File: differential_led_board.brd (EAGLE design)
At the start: 72 x 117 mm, 59 parts, among them IC1 SN75175SOP-16, IC10 TJA1057, IC3 LD1117S33, IC4 74LVC1G157, IC5 74LVC1G157, IC6 CD40109B, IC7 STM32F042F, IC8 AT25SF041, IC9 LT6100, J1 CORTEX_DEBUG_PTH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

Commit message: yes
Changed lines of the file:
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@@
 <attribute name="SPICEPREFIX" value="C" x="13.208" y="103.0732" size="1.778" layer="27" rot="R270" display="off"/>
 </element>
-<element name="IC3" library="lichtenstein_onion" package="SOT223" value="LD1117S33" x="16.3322" y="89.2302" smashed="yes" rot="R180">
+<element name="IC3" library="lichtenstein_onion" package="SOT223" package3d_urn="urn:adsk.eagle:package:29214/2" value="LD1117S33" x="16.3322" y="89.2302" smashed="yes" rot="R180">
 <attribute name="MOUSER" value="926-LM1117MPX3.3NOPB" x="16.3322" y="89.2302" size="1.778" layer="27" rot="R180" display="off"/>
 <attribute name="NAME" x="12.5857" y="87.7443" size="0.8128" layer="25" font="vector" ratio="10" rot="R90"/>

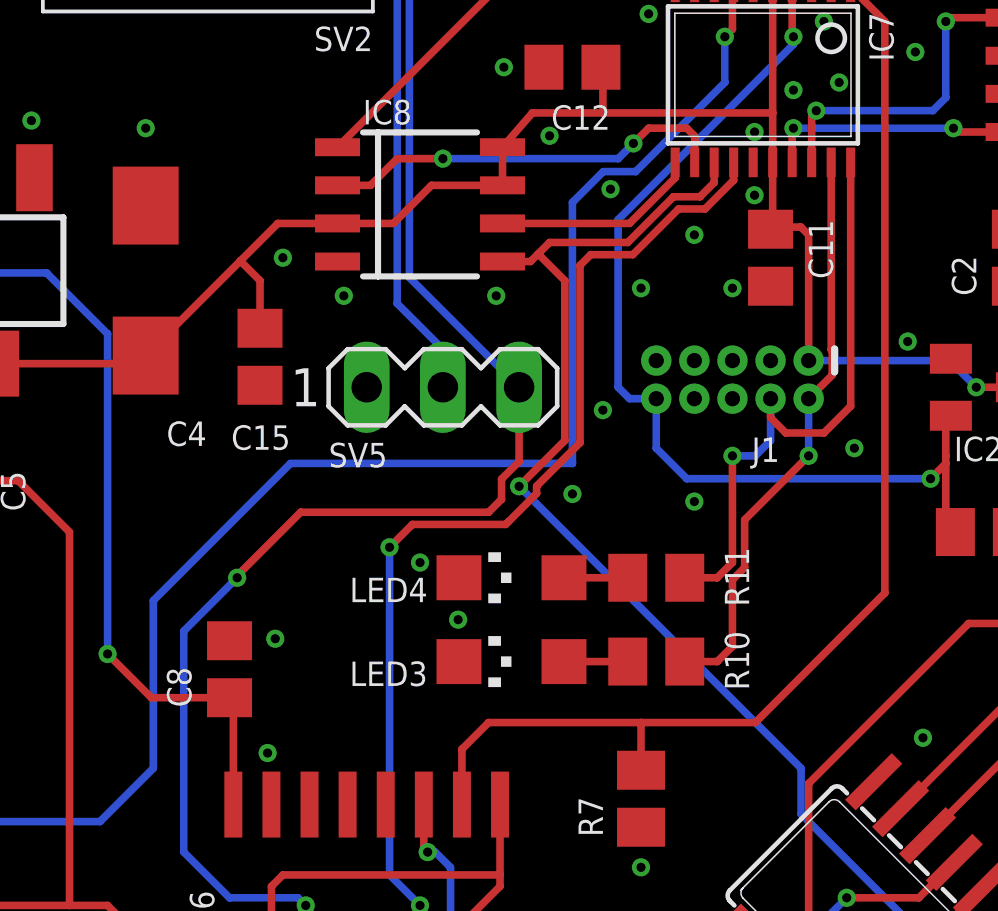
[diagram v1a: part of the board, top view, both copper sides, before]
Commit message: moved status LEDs from debug pins to SPI pins
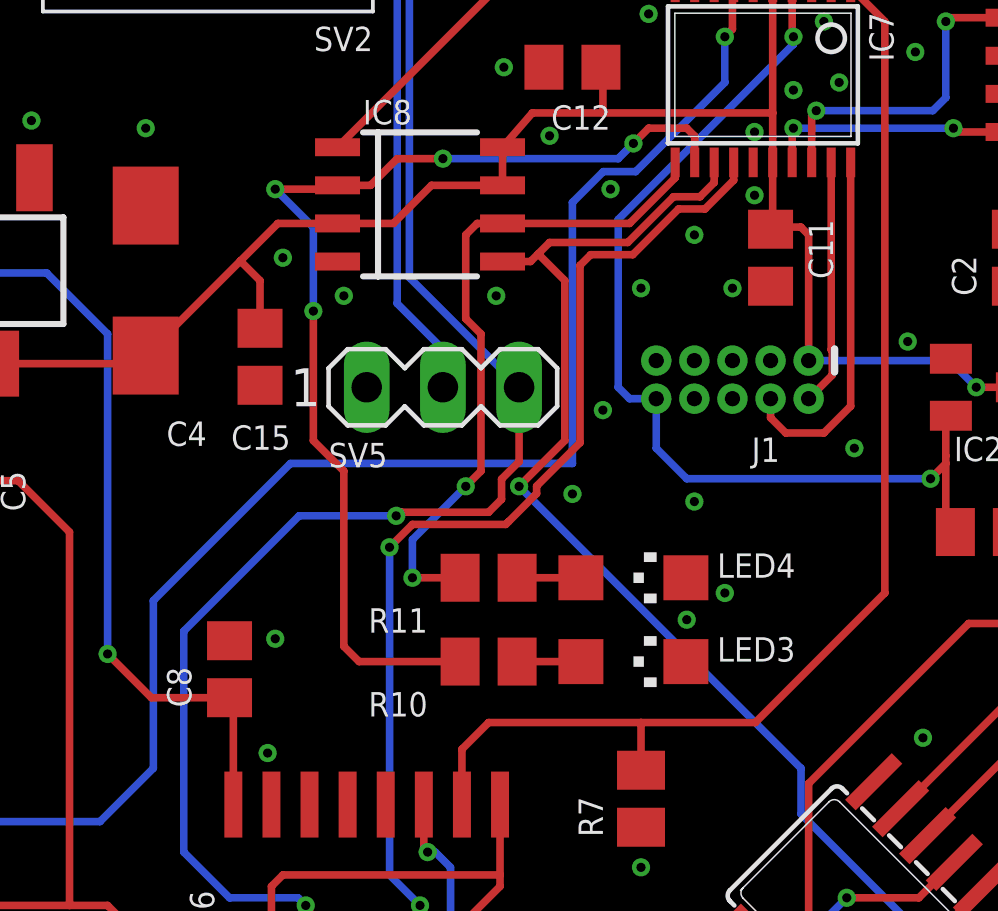
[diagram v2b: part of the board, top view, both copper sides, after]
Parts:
- moved R10 5.59 mm to (33.8, 76.2), turned to 0 degrees
- moved R11 5.59 mm to (33.8, 79.0), turned to 0 degrees
- moved LED3 4.06 mm to (38.6, 76.2), turned to 270 degrees
- moved LED4 4.06 mm to (38.6, 79.0), turned to 270 degrees
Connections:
- net CORTEX_SWCLK: no longer R11.1
- net CORTEX_SWDIO: no longer R10.1
- net SPI_MISO: now also R10.1
- net SPI_SCK: now also R11.1
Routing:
- net SPI_MISO: track 13.7 -> 36.3 mm, vias 2 -> 4
- net SPI_SCK: track 6.90 -> 22.5 mm, vias 0 -> 2
- net CORTEX_SWDIO: track 19.3 -> 8.22 mm, vias 1 -> 0
- net CORTEX_SWCLK: track 20.2 -> 12.0 mm, vias 1 -> 0

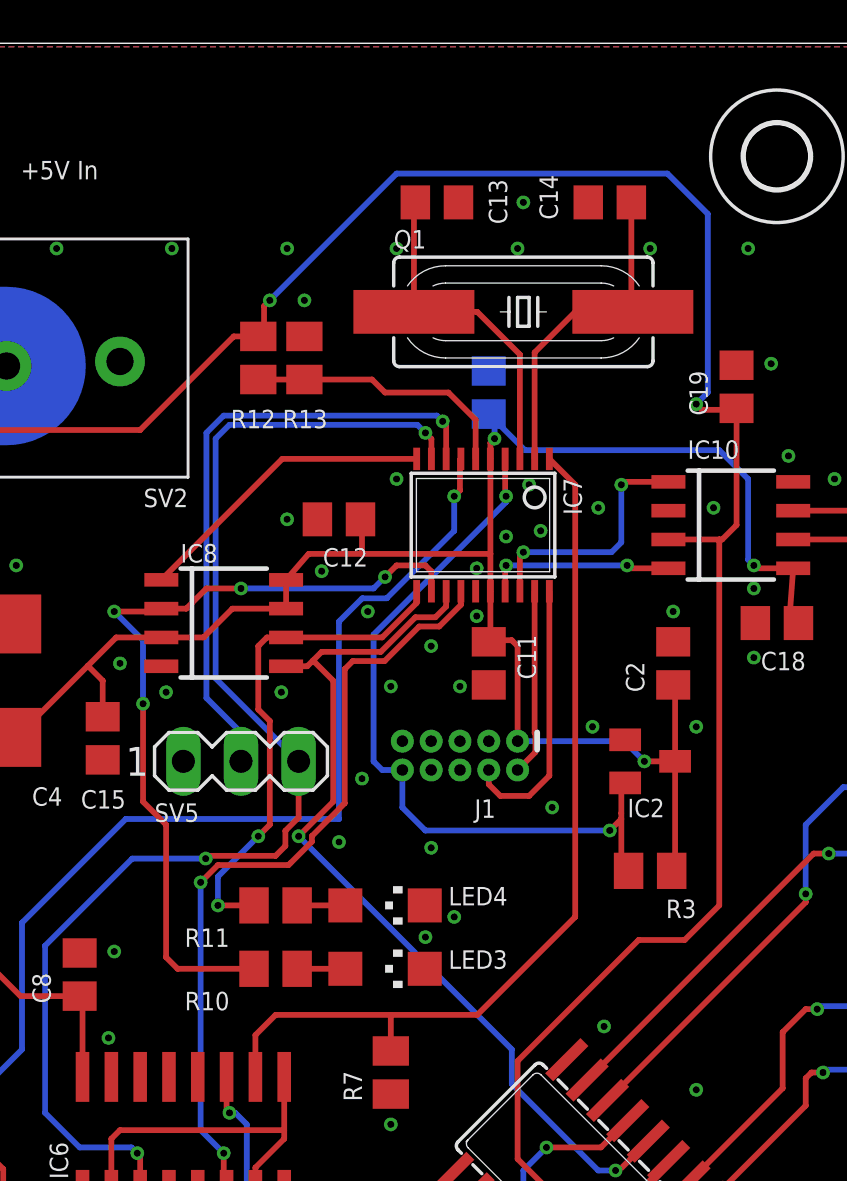
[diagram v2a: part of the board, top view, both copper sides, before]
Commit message: submitted rev 1 of output and led boards to board house
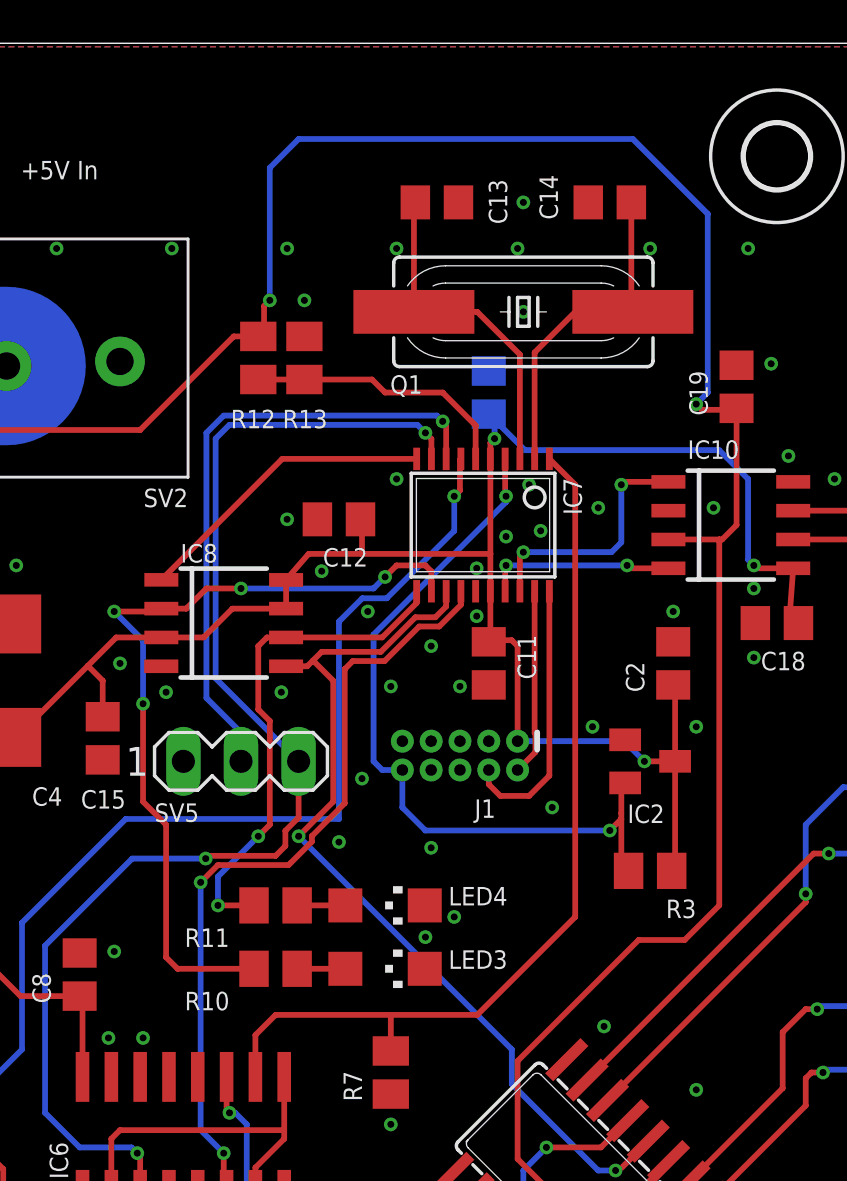
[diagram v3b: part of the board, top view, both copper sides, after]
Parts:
- IC1: value SN75175SOP-16 -> SN75175
- IC2: value (none) -> TLV803
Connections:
- net GND: now also IC6.14
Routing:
- net +5V: track 345.2 -> 349.9 mm
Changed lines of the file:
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@@
 </class>
 </classes>
-<designrules name="dirt_cheap_dirty_boards.v1.1 *">
+<designrules name="dirt_cheap_dirty_boards.v1.1">
 <description language="de">&lt;b&gt;Dirty Cheap Dirty Board Design Rules&lt;/b&gt;
 &lt;br&gt;
@@
 <param name="checkValues" value="0"/>
 <param name="checkNames" value="1"/>
-<param name="checkWireStubs" value="0"/>
+<param name="checkWireStubs" value="1"/>
 <param name="checkPolygonWidth" value="0"/>
 <param name="useDiameter" value="13"/>
@@
 <attribute name="MOUSER" value="449-LFXTAL030234REEL" x="44.704" y="105.156" size="1.778" layer="27" display="off"/>
 <attribute name="MPN" value="" x="44.704" y="105.156" size="1.778" layer="27" display="off"/>
-<attribute name="NAME" x="38.989" y="107.95" size="0.8128" layer="25" font="vector" ratio="10"/>
+<attribute name="NAME" x="40.259" y="102.362" size="0.8128" layer="25" font="vector" ratio="10" rot="R180"/>
 <attribute name="OC_FARNELL" value="unknown" x="44.704" y="105.156" size="1.778" layer="27" display="off"/>
 <attribute name="OC_NEWARK" value="unknown" x="44.704" y="105.156" size="1.778" layer="27" display="off"/>
@@
 <attribute name="SPICEPREFIX" value="C" x="48.514" y="109.982" size="1.778" layer="27" display="off"/>
 </element>
-<element name="IC1" library="lichtenstein_onion" package="SOP-16" value="SN75175SOP-16" x="47.244" y="66.548" smashed="yes" rot="R135">
+<element name="IC1" library="lichtenstein_onion" package="SOP-16" value="SN75175" x="47.244" y="66.548" smashed="yes" rot="R135">
 <attribute name="MOUSER" value="595-SN75175DR" x="47.244" y="66.548" size="1.778" layer="27" rot="R135" display="off"/>
 <attribute name="NAME" x="53.081165625" y="64.302934375" size="0.8128" layer="25" font="vector" ratio="10" rot="R225"/>
@@
 <attribute name="NAME" x="24.638" y="66.929" size="0.8128" layer="25" font="vector" ratio="10" rot="R90"/>
 </element>
-<element name="IC2" library="lichtenstein_onion" package="SOT23" package3d_urn="urn:adsk.eagle:package:28738/2" value="" x="50.292" y="85.344" smashed="yes" rot="R270">
+<element name="IC2" library="lichtenstein_onion" package="SOT23" package3d_urn="urn:adsk.eagle:package:28738/2" value="TLV803" x="50.292" y="85.344" smashed="yes" rot="R270">
 <attribute name="MOUSER" value="595-TLV803SDBZR" x="50.292" y="85.344" size="0.8128" layer="27" font="vector" ratio="10" rot="R270" display="off"/>
-<attribute name="NAME" x="50.927" y="83.693" size="0.8128" layer="25" ratio="10" rot="R180"/>
+<attribute name="NAME" x="50.927" y="83.439" size="0.8128" layer="25" ratio="10" rot="R180"/>
 <attribute name="VALUE" x="47.117" y="87.249" size="1.27" layer="27" rot="R270"/>
 </element>
@@
 <via x="48.006" y="96.52" extent="1-16" drill="0.3048"/>
 <via x="44.704" y="109.982" extent="1-16" drill="0.3048"/>
+<via x="44.704" y="105.156" extent="1-16" drill="0.3048"/>
+<contactref element="IC6" pad="14"/>
+<via x="27.94" y="73.152" extent="1-16" drill="0.3048"/>
 </signal>
 <signal name="+5V">
@@
 <wire x1="33.274" y1="105.41" x2="33.528" y2="105.664" width="0.254" layer="1"/>
 <via x="33.528" y="105.664" extent="1-16" drill="0.3048"/>
-<wire x1="33.528" y1="105.664" x2="39.116" y2="111.252" width="0.254" layer="16"/>
 <wire x1="52.832" y1="101.6" x2="52.324" y2="101.092" width="0.254" layer="16"/>
 <via x="52.324" y="101.092" extent="1-16" drill="0.3048"/>
@@
 <wire x1="52.578" y1="100.838" x2="54.036" y2="100.838" width="0.254" layer="1"/>
 <wire x1="54.036" y1="100.838" x2="54.102" y2="100.904" width="0.254" layer="1"/>
-<wire x1="39.116" y1="111.252" x2="51.054" y2="111.252" width="0.254" layer="16"/>
-<wire x1="51.054" y1="111.252" x2="52.832" y2="109.474" width="0.254" layer="16"/>
+<wire x1="52.832" y1="109.474" x2="49.53" y2="112.776" width="0.254" layer="16"/>
 <wire x1="52.832" y1="109.474" x2="52.832" y2="101.6" width="0.254" layer="16"/>
 <wire x1="47.876859375" y1="60.89468125" x2="50.128246875" y2="58.64329375" width="0.254" layer="1"/>
@@
 <wire x1="51.816" y1="77.47" x2="53.34" y2="78.994" width="0.254" layer="1"/>
 <wire x1="53.34" y1="78.994" x2="53.34" y2="95.123" width="0.254" layer="1"/>
+<wire x1="34.798" y1="112.776" x2="33.528" y2="111.506" width="0.254" layer="16"/>
+<wire x1="49.53" y1="112.776" x2="34.798" y2="112.776" width="0.254" layer="16"/>
+<wire x1="33.528" y1="111.506" x2="33.528" y2="105.664" width="0.254" layer="16"/>
 </signal>
 <signal name="N$1">
@@
 <wire x1="33.02" y1="102.174" x2="35.052" y2="102.174" width="0.254" layer="1"/>
 <wire x1="35.052" y1="102.174" x2="38.034" y2="102.174" width="0.254" layer="1"/>
-<wire x1="42.601" y1="100.401" x2="42.601" y2="98.6758" width="0.254" layer="1"/>
+<wire x1="42.601" y1="100.147" x2="42.601" y2="98.6758" width="0.254" layer="1"/>
 <wire x1="38.034" y1="102.174" x2="38.608" y2="101.6" width="0.254" layer="1"/>
-<wire x1="38.608" y1="101.6" x2="41.402" y2="101.6" width="0.254" layer="1"/>
-<wire x1="41.402" y1="101.6" x2="42.601" y2="100.401" width="0.254" layer="1"/>
+<wire x1="38.608" y1="101.6" x2="41.148" y2="101.6" width="0.254" layer="1"/>
+<wire x1="41.148" y1="101.6" x2="42.601" y2="100.147" width="0.254" layer="1"/>
 </signal>
 <signal name="ADC_CURRENT">

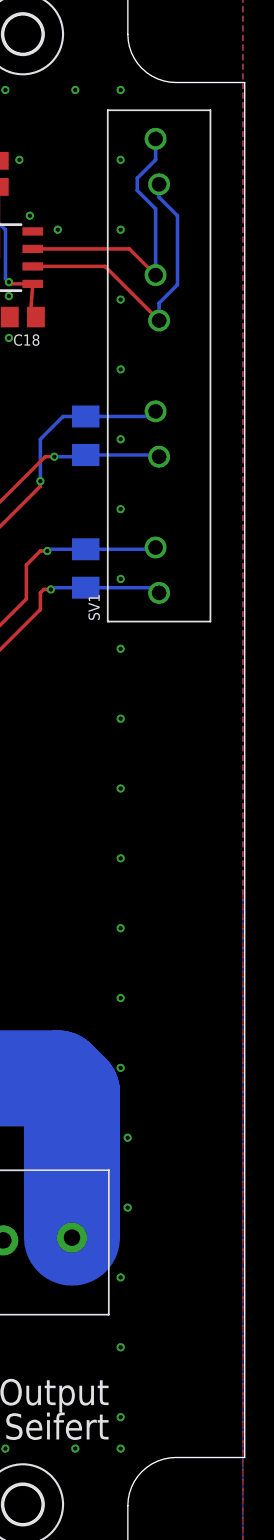
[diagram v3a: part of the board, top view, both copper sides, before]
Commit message: rev01 of output_8ch_spi_mux sent to manufacturing
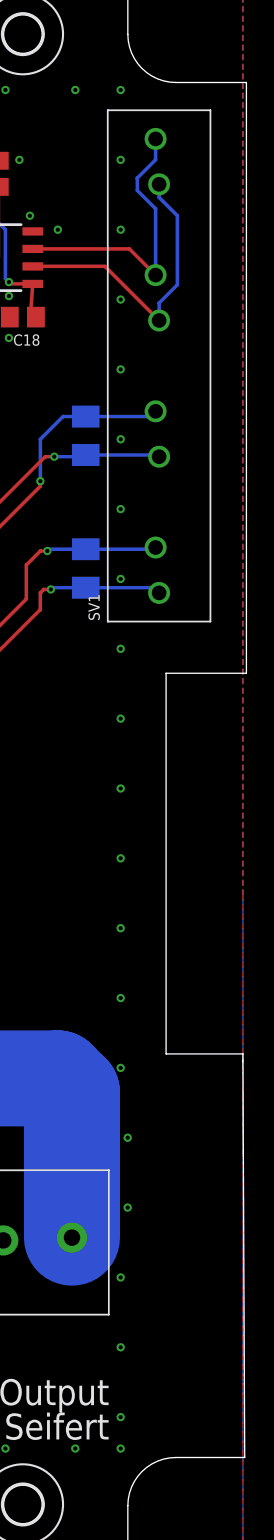
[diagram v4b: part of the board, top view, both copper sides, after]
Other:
- board size 72 x 117 mm -> 72.1 x 117 mm
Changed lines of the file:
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@@
 <wire x1="63.51338125" y1="116.99566875" x2="63.51338125" y2="111.99566875" width="0.001" layer="20"/>
 <wire x1="63.51338125" y1="111.99566875" x2="67.01338125" y2="108.49566875" width="0.001" layer="20" curve="90"/>
-<wire x1="67.01338125" y1="108.49566875" x2="72.01338125" y2="108.49566875" width="0.001" layer="20"/>
-<wire x1="72.01338125" y1="108.49566875" x2="72.01338125" y2="8.49566875" width="0.001" layer="20"/>
+<wire x1="67.01338125" y1="108.49566875" x2="72.136" y2="108.49566875" width="0.001" layer="20"/>
+<wire x1="72.136" y1="108.49566875" x2="72.136" y2="65.532" width="0.001" layer="20"/>
+<wire x1="72.136" y1="65.532" x2="66.294" y2="65.532" width="0.001" layer="20"/>
+<wire x1="66.294" y1="65.532" x2="66.294" y2="37.846" width="0.001" layer="20"/>
+<wire x1="66.294" y1="37.846" x2="71.882" y2="37.846" width="0.001" layer="20"/>
+<wire x1="71.882" y1="37.846" x2="71.882" y2="37.338" width="0.001" layer="20"/>
+<wire x1="71.882" y1="37.338" x2="72.01338125" y2="8.49566875" width="0.001" layer="20"/>
 <wire x1="72.01338125" y1="8.49566875" x2="67.01338125" y2="8.49566875" width="0.001" layer="20"/>
 <wire x1="67.01338125" y1="8.49566875" x2="63.51338125" y2="4.99566875" width="0.001" layer="20" curve="90"/>
